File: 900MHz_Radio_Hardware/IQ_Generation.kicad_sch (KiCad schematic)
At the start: 10 parts, among them Q1 BSS138, Q2 BSS138, U4 74HC165, U8 74LVC1G08, U9 74LVC1G08

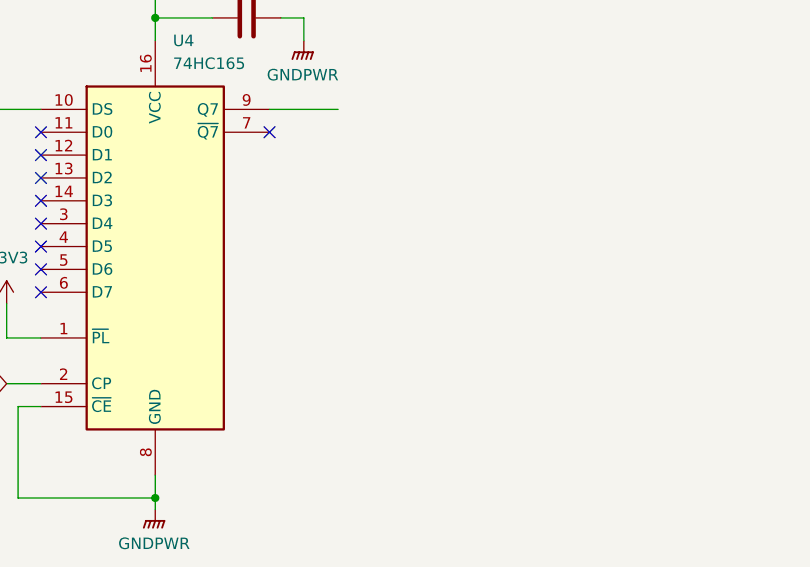
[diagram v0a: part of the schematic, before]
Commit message: Added modulator enable signal
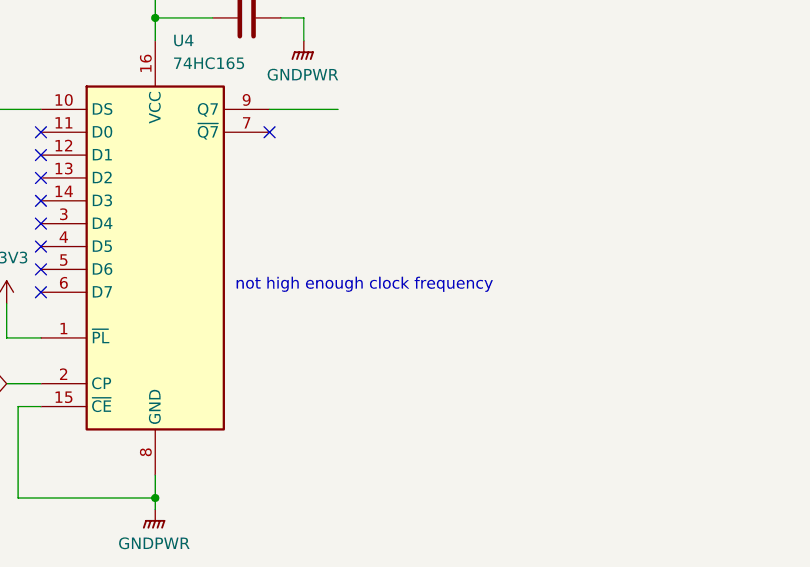
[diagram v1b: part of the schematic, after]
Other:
- note added: "not high enough clock frequency"
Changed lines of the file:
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@@
     (stroke (width 0) (type default))
+  )
+  (text "not high enough clock frequency" (at 152.4 82.55 0)
+    (effects (font (size 1.27 1.27)) (justify left bottom))
   )
   (global_label "SPI_SCK" (shape input) (at 127 92.71 180) (fields_autoplaced)

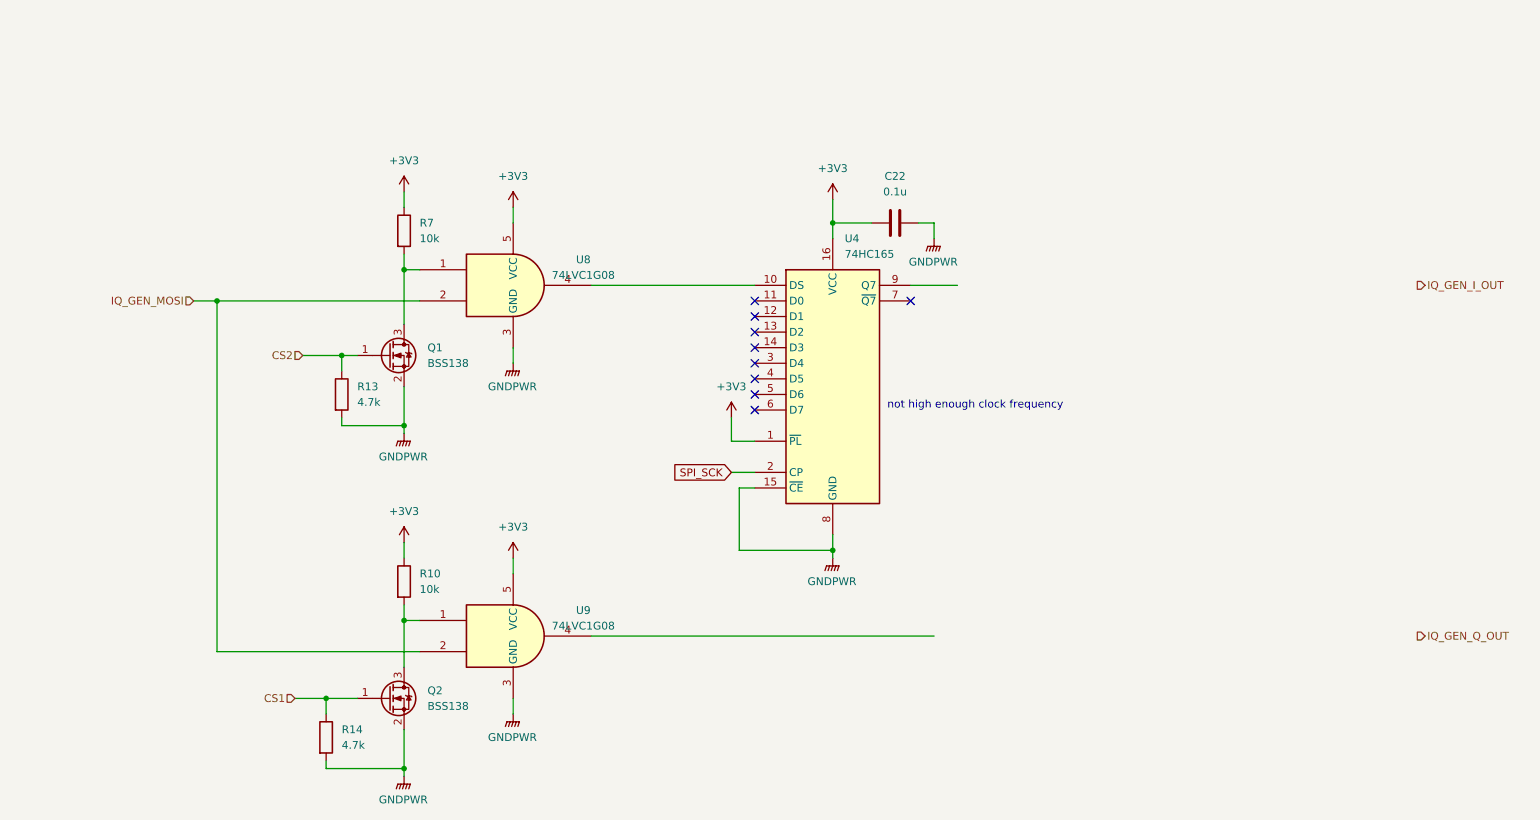
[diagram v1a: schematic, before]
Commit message: Started fixing IQ gen circuit
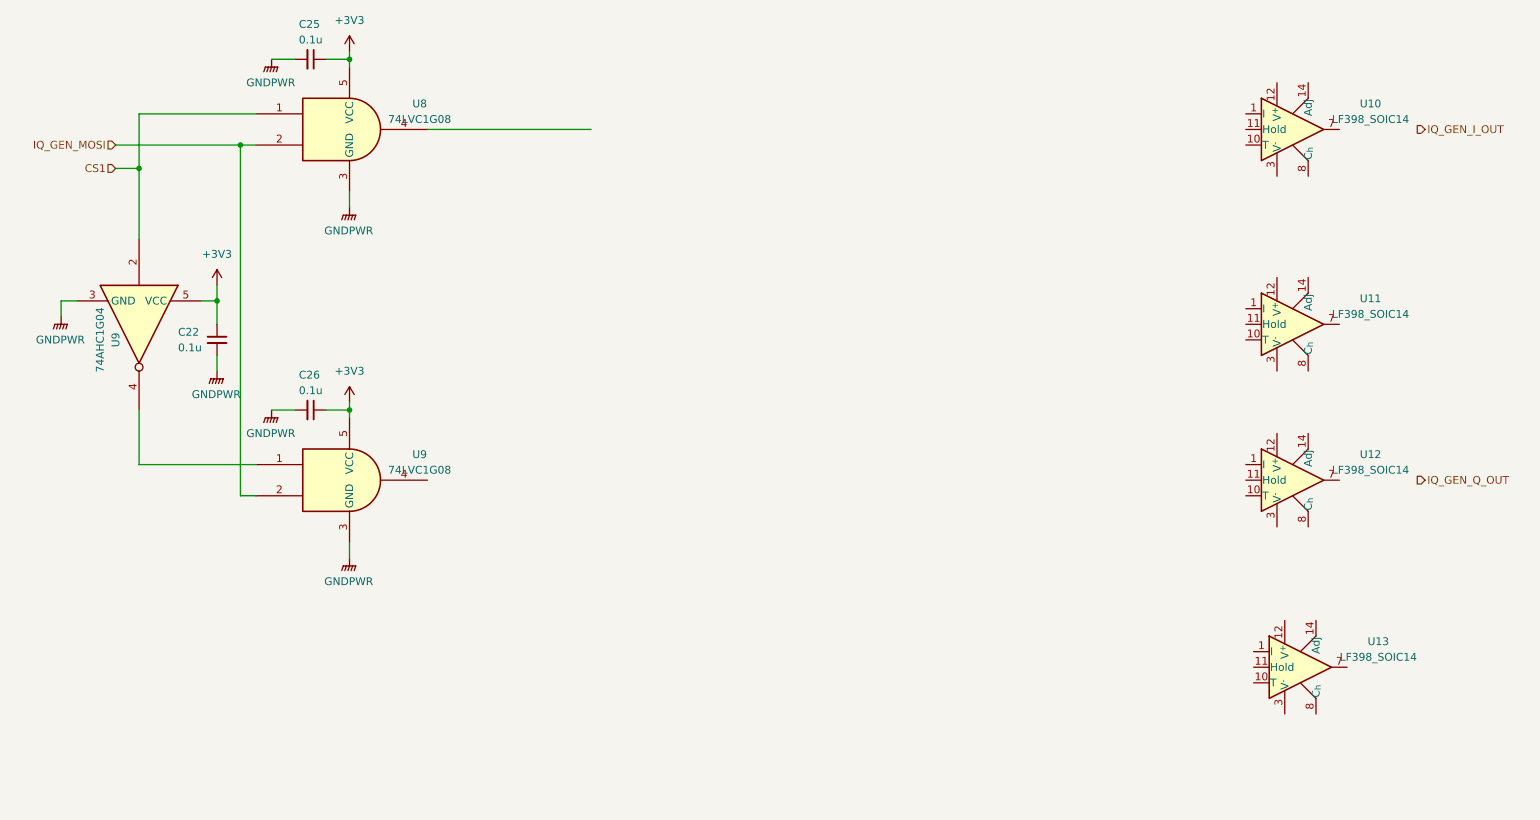
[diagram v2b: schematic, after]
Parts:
- removed C22: 0.1u, symbol Device:C
- removed Q1, Q2: BSS138, Package_TO_SOT_SMD:SOT-23, symbol Transistor_FET:BSS138
- removed R10, R7: 10k, symbol Device:R
- removed R13, R14: 4.7k, symbol Device:R
- removed U4: 74HC165, Package_SO:SOIC-16_3.9x9.9mm_P1.27mm, symbol 74xx:74HC165
- added C22, C25, C26: 0.1u, symbol Device:C_Small
- added U10, U11, U12, U13: LF398_SOIC14, Package_SO:SOIC-14_3.9x8.7mm_P1.27mm, symbol Analog:LF398_SOIC14
- added U9: 74AHC1G04, symbol 74xGxx:74AHC1G04
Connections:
- net +3V3: now also C22.1, C25.1, C26.1, U9.5 (VCC)
- net CS1: now also U8.1, U9.2
- net GNDPWR: now also C22.2, C25.2, C26.2, U9.3 (GND)
- net at U9.1: now also U9.4
- no-connect marks 9 -> 0
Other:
- note removed: "not high enough clock frequency"
- moved on the sheet: U8, U9
